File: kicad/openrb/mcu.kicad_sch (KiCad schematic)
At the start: 35 parts, among them U1 RP2040, U4 RT9080-33, U5 W25Q16JV, X1 12MHz

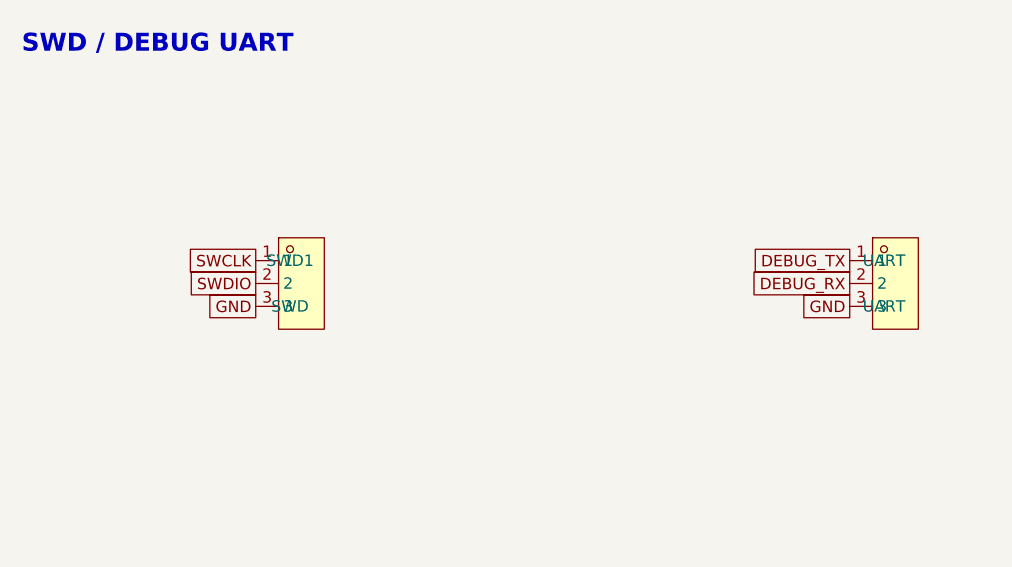
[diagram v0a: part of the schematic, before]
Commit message: Fix SWD1/UART header pinout (GND is the middle/first pin)
Hardware-verified by attaching a CMSIS-DAP SWD probe: both RP2040 cores
enumerate only with GND on SWD1 pin 2 and UART pin 1. Corrects the earlier
reconstruction which had GND on pin 3. Updated the generator, regenerated
the schematic/netlist/PDF, and the spec.
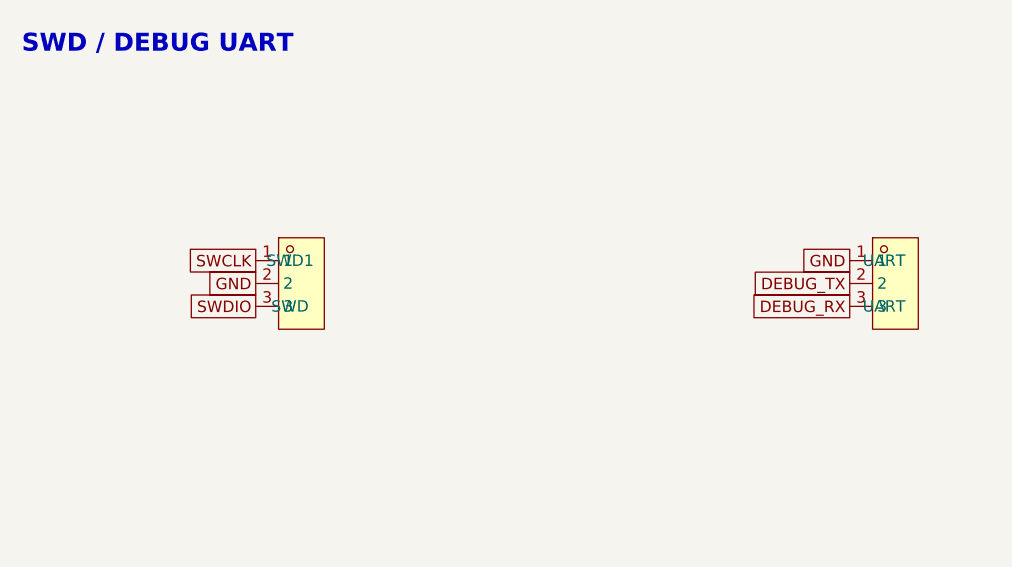
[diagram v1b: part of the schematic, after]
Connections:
- net DEBUG_RX: now also UART.3; no longer UART.2
- net DEBUG_TX: now also UART.2; no longer UART.1
- net GND: now also SWD1.2, UART.1; no longer SWD1.3, UART.3
- net SWDIO: now also SWD1.3; no longer SWD1.2
